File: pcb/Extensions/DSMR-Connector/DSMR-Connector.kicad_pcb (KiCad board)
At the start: 2 copper layers, 31 x 15.2 mm, 5 parts, among them J1 RJ12, J2 Conn_01x04, U1 FOD8012

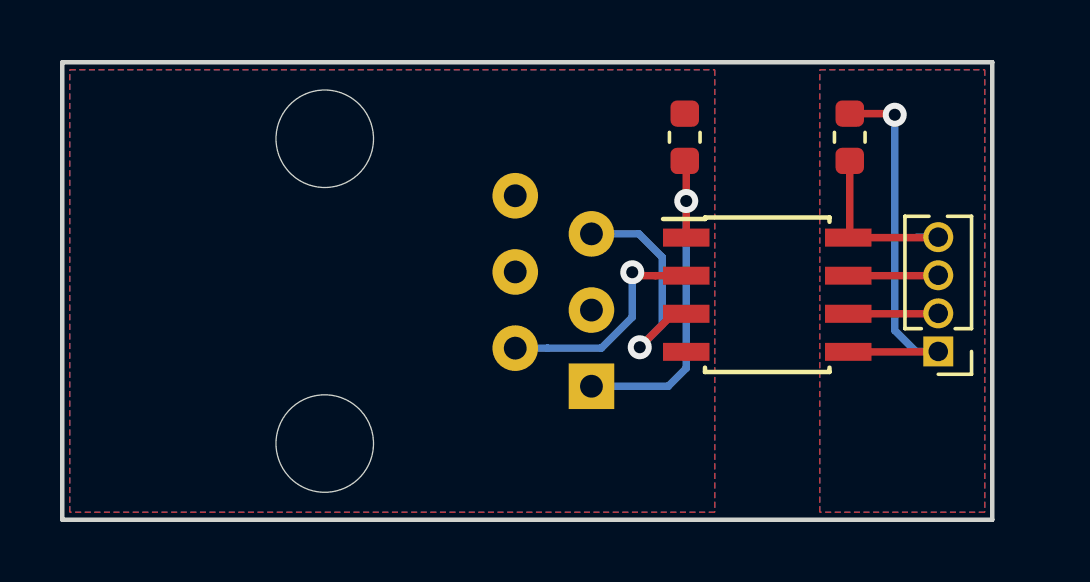
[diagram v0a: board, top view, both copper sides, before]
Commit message: DSMR-Connector v1.1.0
- Add missing pull-up resistor
- Add signal inverter.
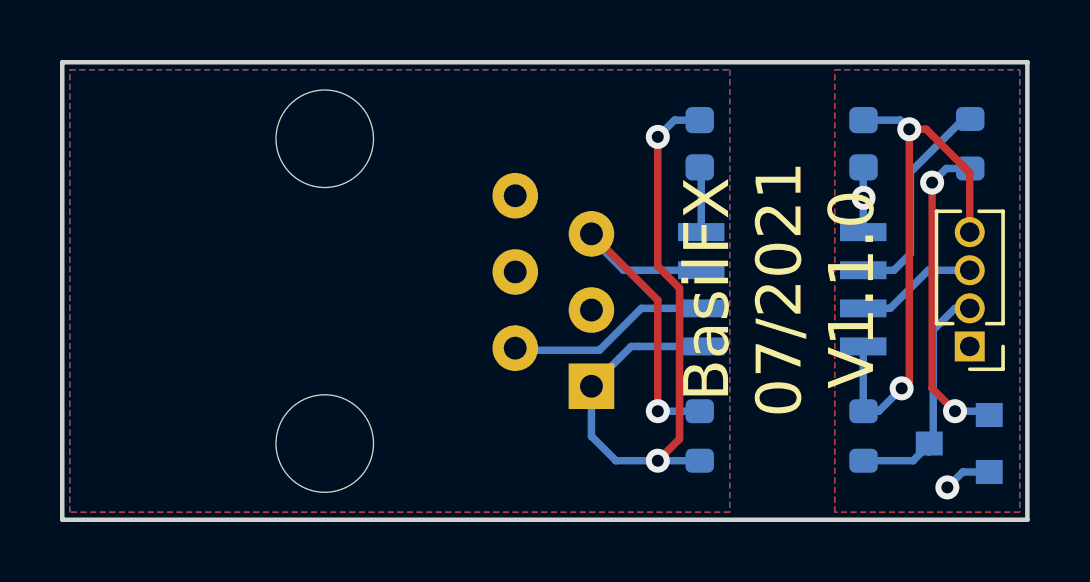
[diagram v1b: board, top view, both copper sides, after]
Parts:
- added Q1: BC847, Package_TO_SOT_SMD:SOT-23, B.Cu at (127.7, 104.7)
- added R1: 10K, Resistor_SMD:R_0603_1608Metric, B.Cu at (119.0, 104.5)
- added R2: 10K, Resistor_SMD:R_0603_1608Metric, B.Cu at (128.0, 94.7)
- added R3: 10K, Resistor_SMD:R_0603_1608Metric, B.Cu at (124.5, 104.5)
- C1, C2: value C -> 100nF; moved to B.Cu
- U1: moved to B.Cu
- moved J2 1.06 mm to (128.0, 101.5)
- moved C1 0.54 mm to (119.0, 94.7), turned to 270 degrees
- moved U1 0.53 mm to (121.8, 99.6)
- moved C2 0.51 mm to (124.5, 94.7), turned to 270 degrees
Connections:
- J2 pad 2: /RX -> /TXn
- U1 pad 6: /RX -> /TX
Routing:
- net VDD: track 6.30 -> 19.0 mm, vias 0 -> 2
- net VDDA: track 12.0 -> 22.8 mm, vias 1 -> 2
- net Net-(Q1-Pad1): track 0.00 -> 10.7 mm, vias 0 -> 2
- net GND: track 13.5 -> 3.77 mm, vias 1 -> 2
- net /TXn: track 0.00 -> 8.04 mm
- net /TX: track 0.00 -> 6.90 mm
- net /TXA: track 8.01 -> 12.4 mm
- net /RX: track 3.01 -> 0.00 mm
- net GNDA: track 0.00 -> 2.09 mm
- net /RTSA: track 8.15 -> 6.85 mm, vias 1 -> 0
- net /RTS: track 3.01 -> 4.08 mm
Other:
- board size 31 x 15.2 mm -> 32.2 x 15.2 mm
- board text added: "BasilFX 07/2021 V1.1.0"
- board text removed: "BasilFX 08/2018 V1.0.0"

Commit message: Upgrade DSMR Connector to KiCad 6.0
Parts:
- J2: moved to B.Cu
- U1: footprint Package_SO:SOIC-8_3.9x4.9mm_P1.27mm -> SMD_Packages:SOIC-8-N
- turned J2 to 0 degrees
- turned U1 to 90 degrees
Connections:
- J1 pad 4: Net-(J1-Pad4) -> unconnected-(J1-Pad4)
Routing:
- net /RTS: track 4.08 -> 3.18 mm
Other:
- net class Default removed
- board text added: "BasilFX 09/2022 V1.2.0"
- board text removed: "BasilFX 07/2021 V1.1.0"
